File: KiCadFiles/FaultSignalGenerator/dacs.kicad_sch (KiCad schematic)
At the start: 8 parts

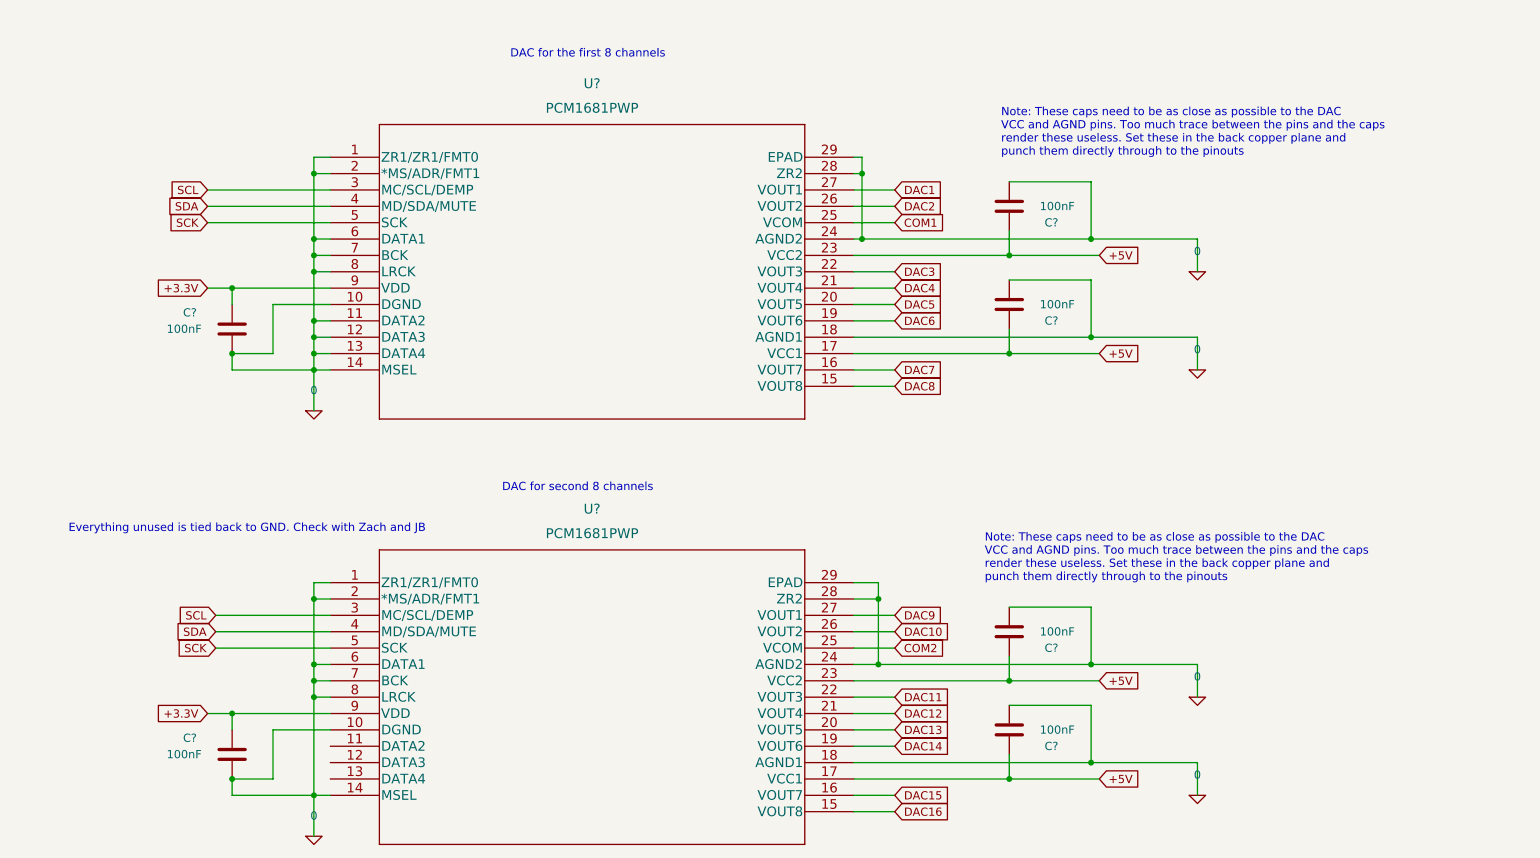
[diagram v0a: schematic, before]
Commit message: Finish schematic, start on PCB
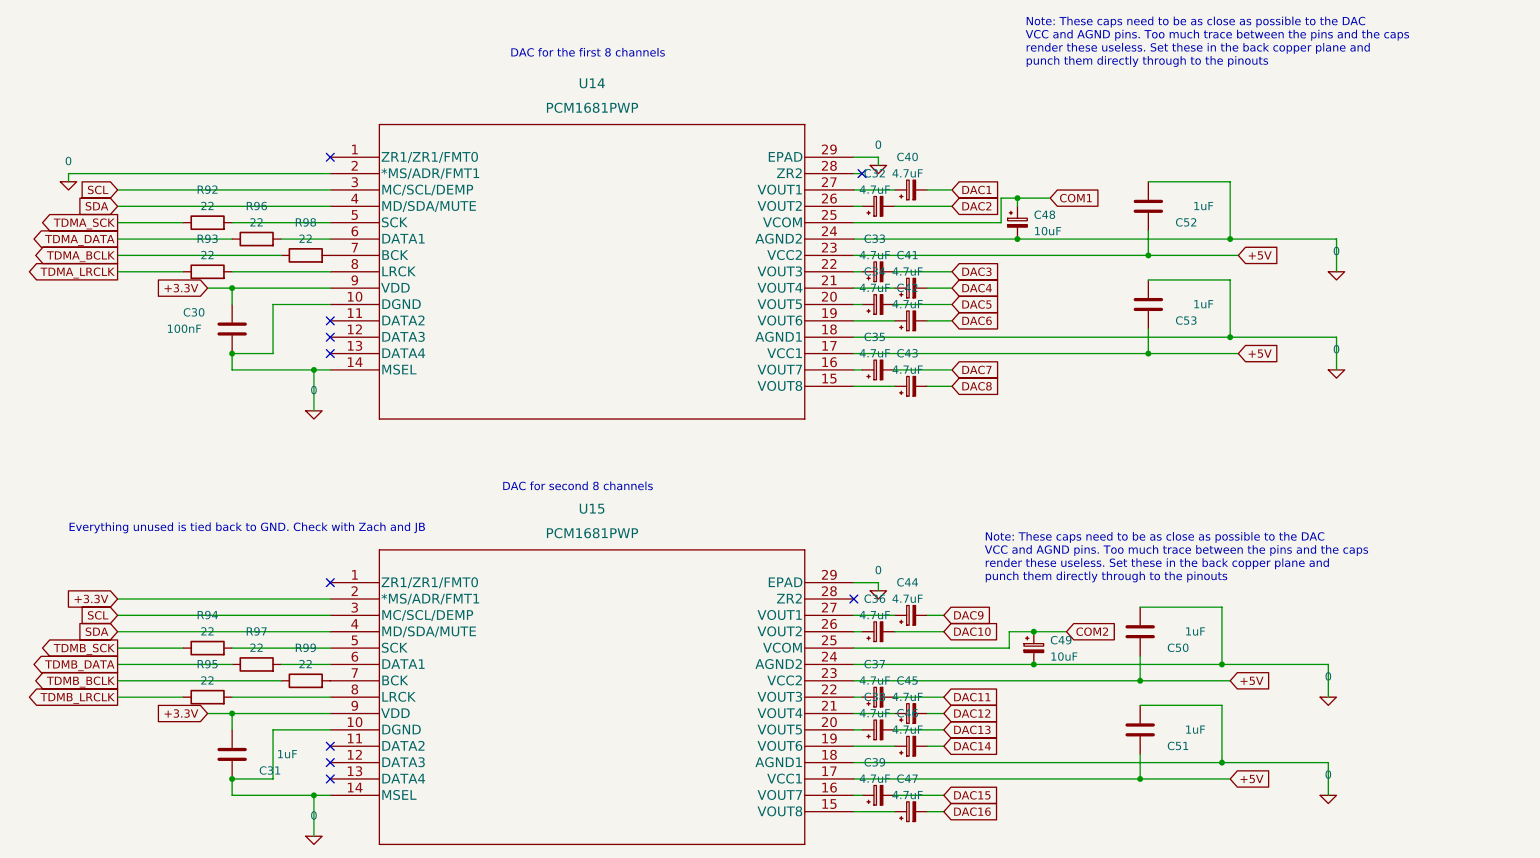
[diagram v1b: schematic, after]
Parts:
- removed C? (x4): 100nF, Capacitor_SMD:C_1812_4532Metric_Pad1.57x3.40mm_HandSolder, symbol Device:C
- added C31, C50, C52, C53: 1uF, Capacitor_SMD:C_1206_3216Metric_Pad1.33x1.80mm_HandSolder, symbol Device:C
- added C32, C33, C34, C35, C36, C37, C38, C39, C40, C41, C42, C43, C44, C45, C46, C47: 4.7uF, Capacitor_SMD:C_1206_3216Metric_Pad1.33x1.80mm_HandSolder, symbol Device:C_Polarized_Small
- added C48, C49: 10uF, Capacitor_SMD:CP_Elec_4x5.4, symbol Device:C_Polarized_Small
- added R92, R93, R94, R95, R96, R97, R98, R99: 22, Resistor_SMD:R_1206_3216Metric, symbol Device:R
- C30: renamed from C?; footprint Capacitor_SMD:C_1812_4532Metric_Pad1.57x3.40mm_HandSolder -> Capacitor_SMD:C_1206_3216Metric_Pad1.33x1.80mm_HandSolder; Spice_Model 4700p -> (none); Spice_Netlist_Enabled Y -> (none); Spice_Primitive C -> (none)
- C51: renamed from C?; value 100nF -> 1uF; footprint Capacitor_SMD:C_1812_4532Metric_Pad1.57x3.40mm_HandSolder -> Capacitor_SMD:C_1206_3216Metric_Pad1.33x1.80mm_HandSolder; Spice_Model 4700p -> (none); Spice_Netlist_Enabled Y -> (none); Spice_Primitive C -> (none)
- U14, U15: renamed from U?; footprint PCM1681PWP:PCM1681PWP -> Package_SO:HTSSOP-28-1EP_4.4x9.7mm_P0.65mm_EP2.85x5.4mm
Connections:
- net +3.3V: now also U15.2 (*MS/ADR/FMT1), C31.2
- net +5V: now also C50.1, C52.1, C53.1
- net 0: now also C31.1, C48.2, C49.2, C50.2, C52.2, C53.2; no longer U14.1 (ZR1/ZR1/FMT0), U14.11 (DATA2), U14.12 (DATA3), U14.13 (DATA4), U14.28 (ZR2), U14.6 (DATA1), U14.7 (BCK), U14.8 (LRCK), U15.1 (ZR1/ZR1/FMT0), U15.2 (*MS/ADR/FMT1), U15.28 (ZR2), U15.6 (DATA1), U15.7 (BCK), U15.8 (LRCK)
- net COM1: now also C48.1
- net COM2: now also C49.1
- net DAC1: now also C40.2; no longer U14.27 (VOUT1)
- net DAC10: now also C36.2; no longer U15.26 (VOUT2)
- net DAC11: now also C37.2; no longer U15.22 (VOUT3)
- net DAC12: now also C45.2; no longer U15.21 (VOUT4)
- net DAC13: now also C38.2; no longer U15.20 (VOUT5)
- net DAC14: now also C46.2; no longer U15.19 (VOUT6)
- net DAC15: now also C39.2; no longer U15.16 (VOUT7)
- net DAC16: now also C47.2; no longer U15.15 (VOUT8)
- net DAC2: now also C32.2; no longer U14.26 (VOUT2)
- net DAC3: now also C33.2; no longer U14.22 (VOUT3)
- net DAC4: now also C41.2; no longer U14.21 (VOUT4)
- net DAC5: now also C34.2; no longer U14.20 (VOUT5)
- net DAC6: now also C42.2; no longer U14.19 (VOUT6)
- net DAC7: now also C35.2; no longer U14.16 (VOUT7)
- net DAC8: now also C43.2; no longer U14.15 (VOUT8)
- net DAC9: now also C44.2; no longer U15.27 (VOUT1)
- net SCK: no longer names the net of U15.5 (SCK)
- net SCK: now also R94.2; no longer U14.5 (SCK)
- new net: C45.1, U15.21 (VOUT4)
- new net: C47.1, U15.15 (VOUT8)
- new net: C39.1, U15.16 (VOUT7)
- new net: C46.1, U15.19 (VOUT6)
- new net: C38.1, U15.20 (VOUT5)
- new net: C37.1, U15.22 (VOUT3)
- new net: C36.1, U15.26 (VOUT2)
- new net: C44.1, U15.27 (VOUT1)
- new net: R97.2, U15.6 (DATA1)
- new net: R99.2, U15.7 (BCK)
- new net: R95.2, U15.8 (LRCK)
- new net: R93.2, U14.8 (LRCK)
- new net: C41.1, U14.21 (VOUT4)
- new net: R98.2, U14.7 (BCK)
- new net: C43.1, U14.15 (VOUT8)
- new net: C35.1, U14.16 (VOUT7)
- new net: C42.1, U14.19 (VOUT6)
- new net: C34.1, U14.20 (VOUT5)
- new net: C33.1, U14.22 (VOUT3)
- new net: C32.1, U14.26 (VOUT2)
- new net: C40.1, U14.27 (VOUT1)
- new net: R92.2, U14.5 (SCK)
- new net: R96.2, U14.6 (DATA1)
- new net TDMA_BCLK: R98.1
- new net TDMA_DATA: R96.1
- new net TDMA_LRCLK: R93.1
- new net TDMA_SCK: R92.1
- new net TDMB_BCLK: R99.1
- new net TDMB_DATA: R97.1
- new net TDMB_LRCLK: R95.1
- new net TDMB_SCK: R94.1
- no-connect marks 0 -> 10
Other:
- moved on the sheet: C51

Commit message: finish layout
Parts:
- C48, C49: footprint Capacitor_SMD:CP_Elec_4x5.4 -> Capacitor_SMD:C_1206_3216Metric_Pad1.33x1.80mm_HandSolder
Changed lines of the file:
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@@
       (effects (font (size 1.27 1.27)) (justify left))
     )
-    (property "Footprint" "Capacitor_SMD:CP_Elec_4x5.4" (at 209.55 116.84 0)
+    (property "Footprint" "Capacitor_SMD:C_1206_3216Metric_Pad1.33x1.80mm_HandSolder" (at 209.55 116.84 0)
       (effects (font (size 1.27 1.27)) hide)
     )
@@
       (effects (font (size 1.27 1.27)) (justify left))
     )
-    (property "Footprint" "Capacitor_SMD:CP_Elec_4x5.4" (at 207.01 50.8 0)
+    (property "Footprint" "Capacitor_SMD:C_1206_3216Metric_Pad1.33x1.80mm_HandSolder" (at 207.01 50.8 0)
       (effects (font (size 1.27 1.27)) hide)
     )
